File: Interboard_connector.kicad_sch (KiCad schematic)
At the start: 2 parts, among them J1 Chainbus In, J2 Chainbus Out

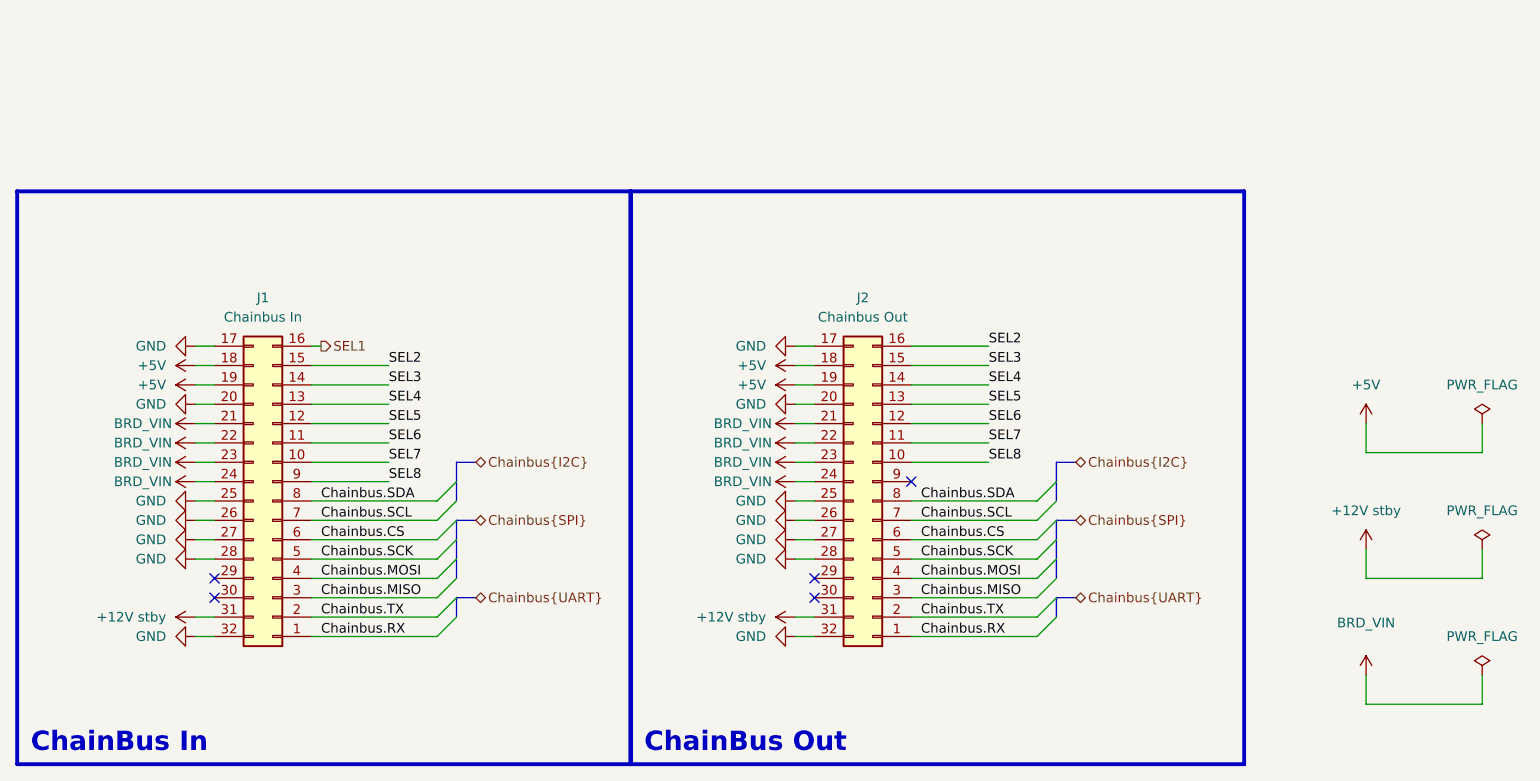
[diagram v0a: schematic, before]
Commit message: Added mechanical standard and updated readme
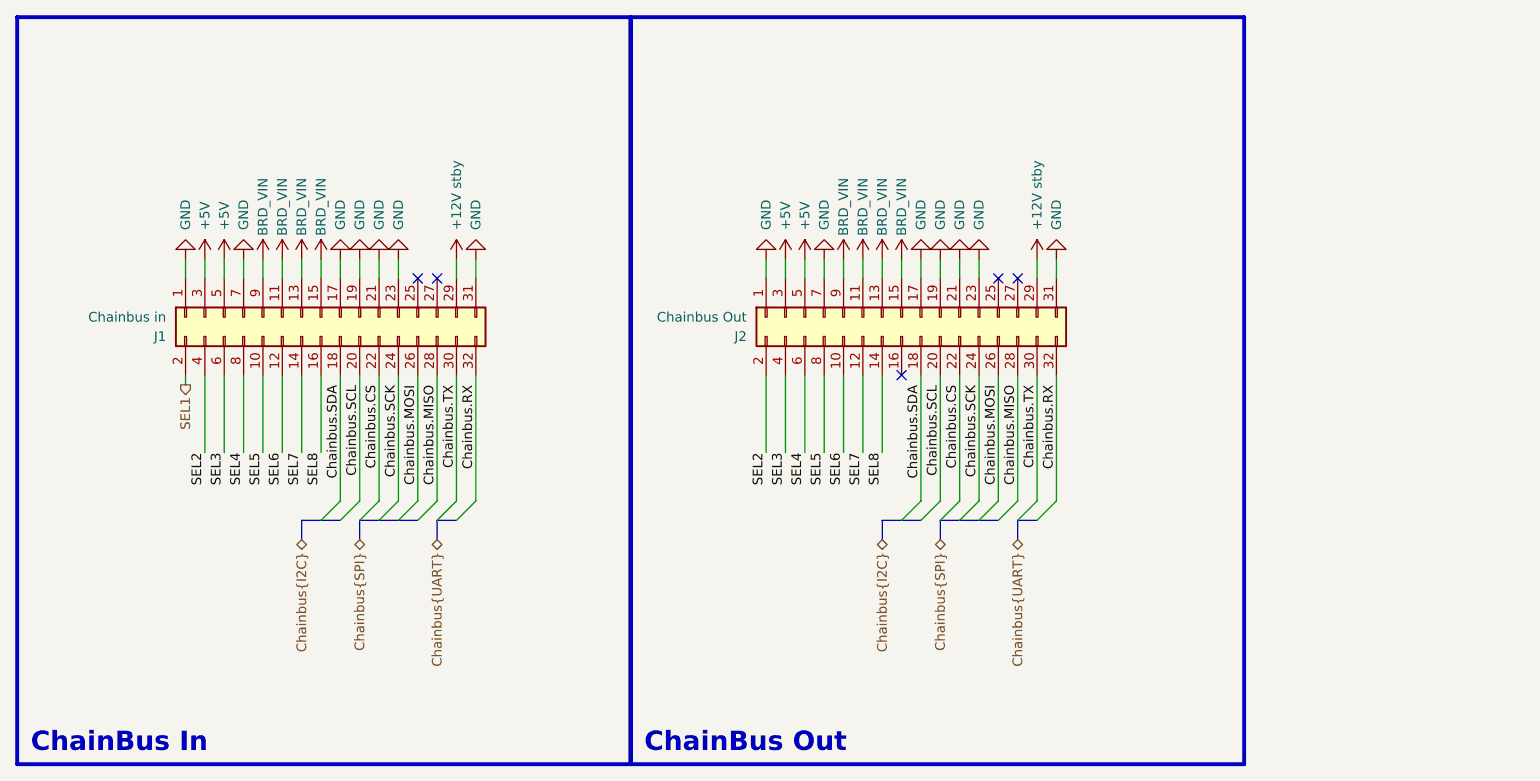
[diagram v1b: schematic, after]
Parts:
- removed J1: Chainbus In, Connector_PinSocket_2.54mm:PinSocket_2x16_P2.54mm_Vertical_SMD, symbol Connector_Generic:Conn_02x16_Counter_Clockwise
- removed J2: Chainbus Out, Connector_PinSocket_2.54mm:PinSocket_2x16_P2.54mm_Vertical_SMD, symbol Connector_Generic:Conn_02x16_Counter_Clockwise
- added J1: Chainbus in, Connector_PinHeader_2.54mm:PinHeader_2x16_P2.54mm_Vertical_SMD, symbol Connector_Generic:Conn_02x16_Odd_Even
- added J2: Chainbus Out, Connector_PinSocket_2.54mm:PinSocket_2x16_P2.54mm_Vertical_SMD, symbol Connector_Generic:Conn_02x16_Odd_Even
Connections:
- net +12V stby: now also J1.29 (Pin_29), J2.29 (Pin_29)
- net +5V: now also J1.3 (Pin_3), J1.5 (Pin_5), J2.3 (Pin_3), J2.5 (Pin_5)
- net BRD_VIN: now also J1.11 (Pin_11), J1.13 (Pin_13), J1.15 (Pin_15), J1.9 (Pin_9), J2.11 (Pin_11), J2.13 (Pin_13), J2.15 (Pin_15), J2.9 (Pin_9)
- net Chainbus.CS: now also J1.22 (Pin_22), J2.22 (Pin_22)
- net Chainbus.MISO: now also J1.28 (Pin_28), J2.28 (Pin_28)
- net Chainbus.MOSI: now also J1.26 (Pin_26), J2.26 (Pin_26)
- net Chainbus.RX: now also J1.32 (Pin_32), J2.32 (Pin_32)
- net Chainbus.SCK: now also J1.24 (Pin_24), J2.24 (Pin_24)
- net Chainbus.SCL: now also J1.20 (Pin_20), J2.20 (Pin_20)
- net Chainbus.SDA: now also J1.18 (Pin_18), J2.18 (Pin_18)
- net Chainbus.TX: now also J1.30 (Pin_30), J2.30 (Pin_30)
- net GND: now also J1.1 (Pin_1), J1.17 (Pin_17), J1.19 (Pin_19), J1.21 (Pin_21), J1.23 (Pin_23), J1.31 (Pin_31), J1.7 (Pin_7), J2.1 (Pin_1), J2.17 (Pin_17), J2.19 (Pin_19), J2.21 (Pin_21), J2.23 (Pin_23), J2.31 (Pin_31), J2.7 (Pin_7)
- net SEL1: now also J1.2 (Pin_2)
- net SEL2: now also J1.4 (Pin_4), J2.2 (Pin_2)
- net SEL3: now also J1.6 (Pin_6), J2.4 (Pin_4)
- net SEL4: now also J1.8 (Pin_8), J2.6 (Pin_6)
- net SEL5: now also J1.10 (Pin_10), J2.8 (Pin_8)
- net SEL6: now also J1.12 (Pin_12), J2.10 (Pin_10)
- net SEL7: now also J1.14 (Pin_14), J2.12 (Pin_12)
- net SEL8: now also J1.16 (Pin_16), J2.14 (Pin_14)
